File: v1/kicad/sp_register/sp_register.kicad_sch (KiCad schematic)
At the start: 5 parts, among them U1 LNCPU Type B Connector, U2 74LS169, U3 74LS169, U4 74LS244, U5 74LS00

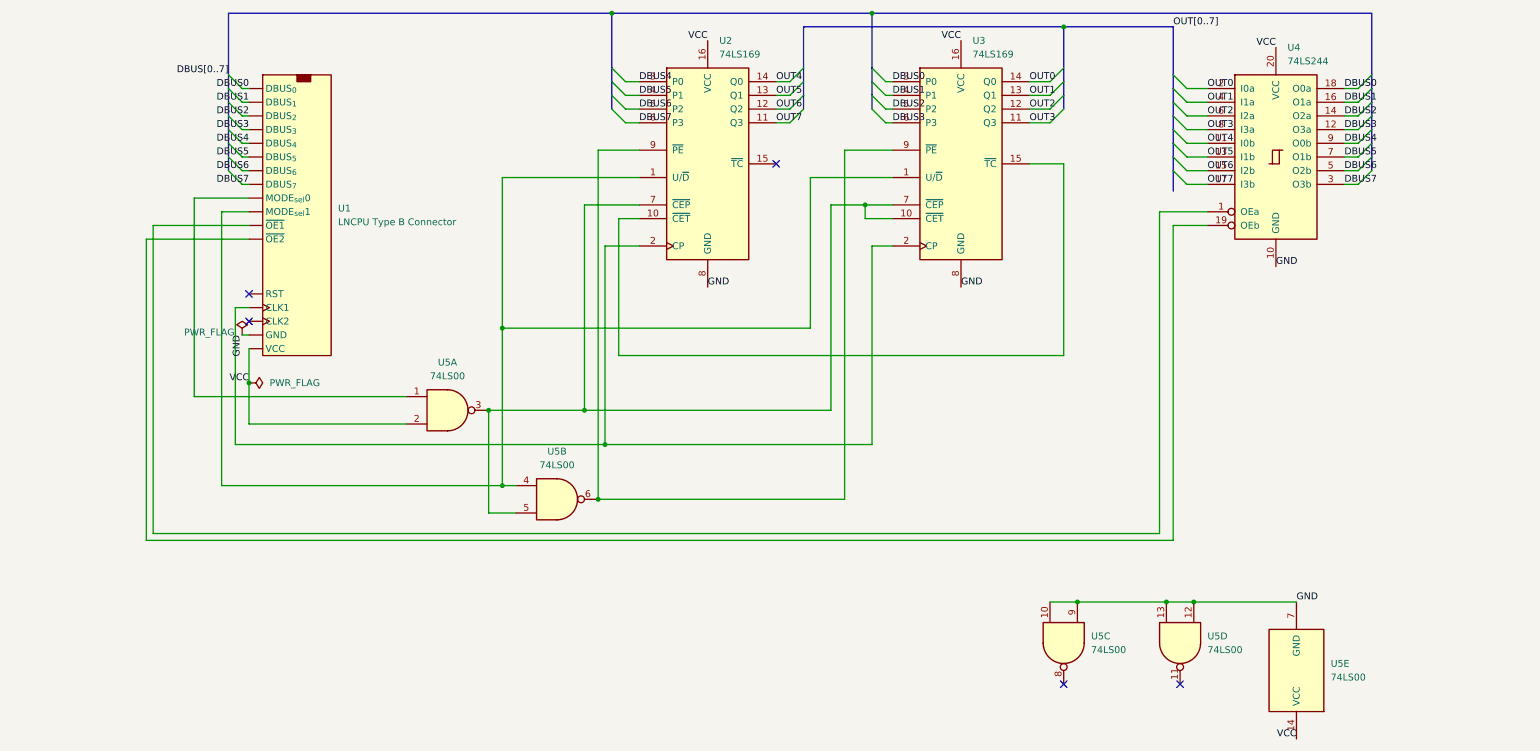
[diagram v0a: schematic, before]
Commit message: check designs for ALU (partial), SP, Shift register, register
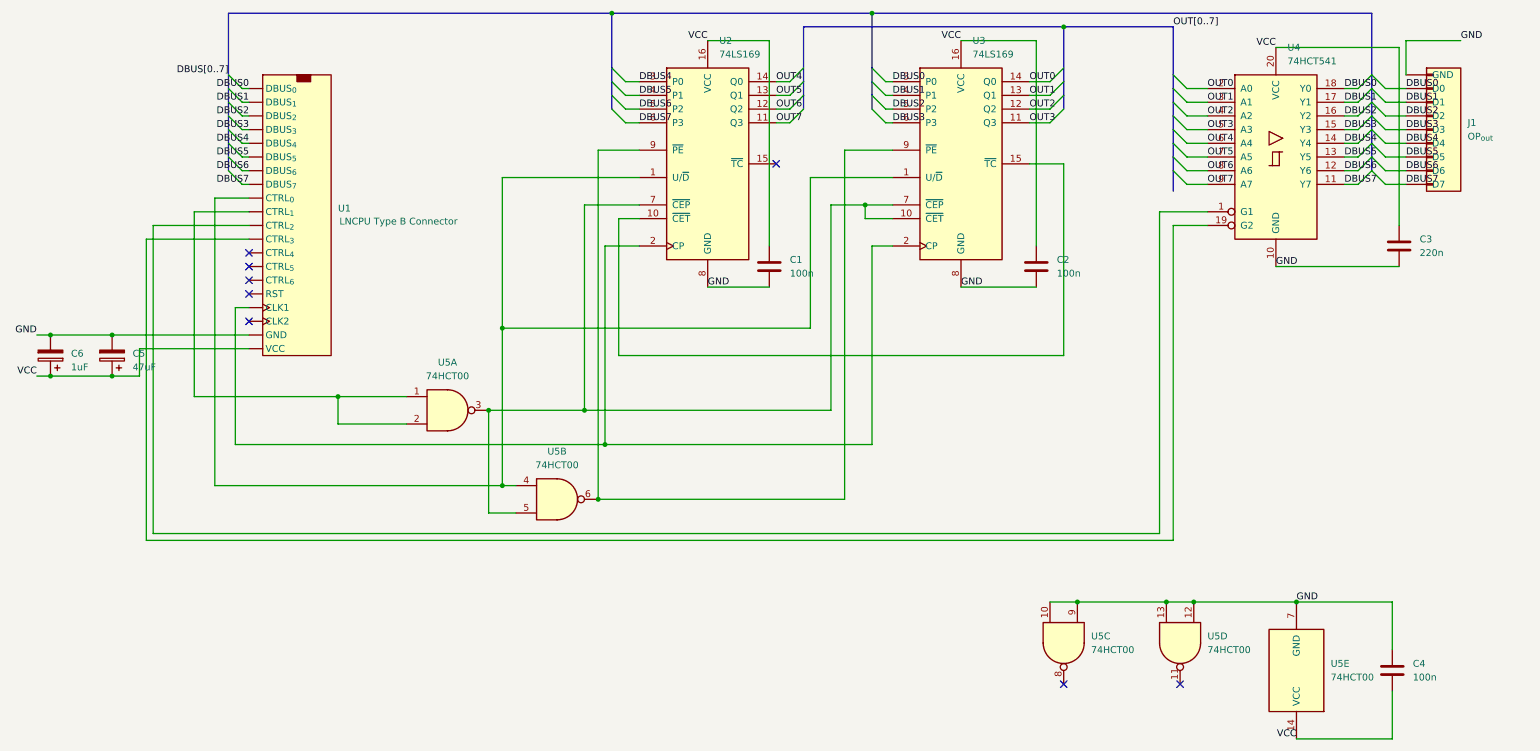
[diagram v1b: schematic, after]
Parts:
- added C1, C2, C4: 100n, Capacitor_THT:C_Disc_D5.0mm_W2.5mm_P5.00mm, symbol Device:C
- added C3: 220n, Capacitor_THT:C_Disc_D5.0mm_W2.5mm_P5.00mm, symbol Device:C
- added C5: 47uF, Capacitor_THT:CP_Radial_D5.0mm_P2.00mm, symbol Device:C_Polarized
- added C6: 1uF, lncpu:CP_Radial_D4.0mm_P2.00mm-Large-Holes, symbol Device:C_Polarized
- added J1: OP_{out}, Connector_PinSocket_2.54mm:PinSocket_1x10_P2.54mm_Vertical, symbol lncpu:LNCPU_8B_Socket
- U1: symbol lncpu:LNCPU_Type_B_Connector -> lncpu:LNCPU_Type_B_Header
- U3: footprint (none) -> Package_DIP:DIP-16_W7.62mm_LongPads
- U4: value 74LS244 -> 74HCT541; symbol 74xx:74LS244 -> 74xx:74HCT541
- U5: value 74LS00 -> 74HCT00; symbol 74xx:74LS00 -> 74xx:74HCT00
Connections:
- net DBUS0: now also J1.2 (D0)
- net DBUS1: now also U4.17 (Y1), J1.3 (D1); no longer U4.16 (O1a)
- net DBUS2: now also U4.16 (Y2), J1.4 (D2); no longer U4.14 (O2a)
- net DBUS3: now also U4.15 (Y3), J1.5 (D3); no longer U4.12 (O3a)
- net DBUS4: now also U4.14 (Y4), J1.6 (D4); no longer U4.9 (O0b)
- net DBUS5: now also U4.13 (Y5), J1.7 (D5); no longer U4.7 (O1b)
- net DBUS6: now also U4.12 (Y6), J1.8 (D6); no longer U4.5 (O2b)
- net DBUS7: now also U4.11 (Y7), J1.9 (D7); no longer U4.3 (O3b)
- net GND: now also C1.2, C2.2, C3.2, C4.1, C5.2, C6.2, J1.1 (GND), J1.10 (GND)
- net OUT1: now also U4.3 (A1); no longer U4.4 (I1a)
- net OUT2: now also U4.4 (A2); no longer U4.6 (I2a)
- net OUT3: now also U4.5 (A3); no longer U4.8 (I3a)
- net OUT4: now also U4.6 (A4); no longer U4.11 (I0b)
- net OUT5: now also U4.7 (A5); no longer U4.13 (I1b)
- net OUT6: now also U4.8 (A6); no longer U4.15 (I2b)
- net OUT7: now also U4.9 (A7); no longer U4.17 (I3b)
- net VCC: now also C1.1, C2.1, C3.1, C4.2, C5.1, C6.1; no longer U5.2
- net at U5.1: now also U1.5 (CTRL_{1}), U5.2; no longer U1.3 (MODE_{sel}0)
- net at U2.1 (U/~{D}), U3.1 (U/~{D}), U5.4: now also U1.3 (CTRL_{0}); no longer U1.5 (MODE_{sel}1)
- no-connect marks 5 -> 8

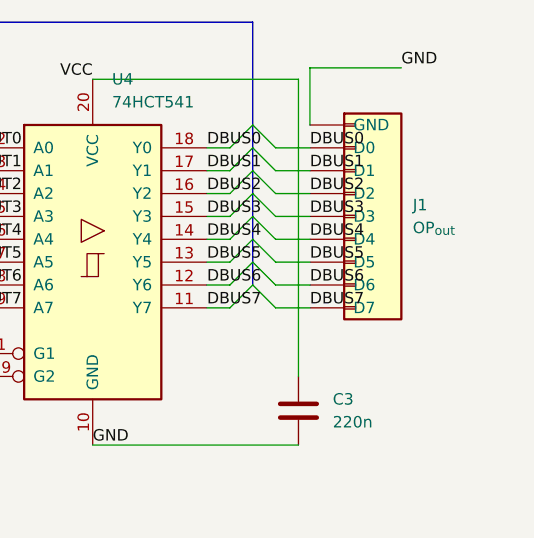
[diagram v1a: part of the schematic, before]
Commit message: readapt designs for BR, SP, SR, ALU
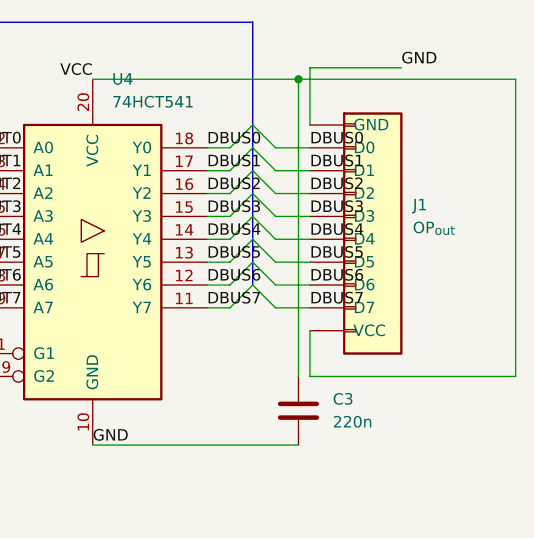
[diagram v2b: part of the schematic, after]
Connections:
- net GND: no longer J1.10 (GND)
- net VCC: now also J1.10 (VCC)
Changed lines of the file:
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@@
 	)
 	(junction
+		(at 275.59 22.86)
+		(diameter 0)
+		(color 0 0 0 0)
+	)
+	(junction
 		(at 127 106.68)
 		(diameter 0)
@@
 	(wire
 		(pts
+			(xy 275.59 22.86) (xy 299.72 22.86)
+		)
+		(stroke
+			(width 0)
+			(type default)
+		)
+	)
+	(wire
+		(pts
 			(xy 207.01 29.21) (xy 210.82 29.21)
 		)
@@
 	(wire
 		(pts
+			(xy 276.86 50.8) (xy 276.86 55.88)
+		)
+		(stroke
+			(width 0)
+			(type default)
+		)
+	)
+	(wire
+		(pts
 			(xy 36.83 76.2) (xy 62.23 76.2)
 		)
@@
 	(wire
 		(pts
+			(xy 276.86 55.88) (xy 299.72 55.88)
+		)
+		(stroke
+			(width 0)
+			(type default)
+		)
+	)
+	(wire
+		(pts
 			(xy 109.22 104.14) (xy 111.76 104.14)
 		)
@@
 	(wire
 		(pts
+			(xy 299.72 55.88) (xy 299.72 22.86)
+		)
+		(stroke
+			(width 0)
+			(type default)
+		)
+	)
+	(wire
+		(pts
 			(xy 124.46 90.17) (xy 124.46 52.07)
 		)
@@
 		(on_board yes)
 		(dnp no)
-		(fields_autoplaced yes)
 		(property "Reference" "J1"
 			(at 288.29 36.8299 0)
